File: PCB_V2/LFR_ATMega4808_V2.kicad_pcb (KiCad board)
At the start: 2 copper layers, 51.7 x 63.4 mm, 78 parts, among them J1 Conn_02x02_Odd_Even, J2 Conn_02x05_Odd_Even, J3 Conn_02x02_Counter_Clockwise, J4 Conn_02x02_Counter_Clockwise, J5 Conn_02x02_Counter_Clockwise, J6 Conn_02x03_Odd_Even, J7 Conn_02x02_Odd_Even, Q1 PMOS, Q2 NMOS, Q3 NMOS, Q4 NMOS, Q5 NMOS, Q6 NMOS, Q6 PMOS, Q7 NMOS, Q8 NMOS, U1 ATmega4808-A, U5 MCP1700x-330xxTO

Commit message: Rough layout done
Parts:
- removed the Q6 at (116.6, 106.2)
- removed the Q6 at (107.7, 93.2)
- removed the Q7 at (107.7, 97.7)
- removed the Q7 at (116.5, 110.6)
- removed the R27 at (102.9, 92.5)
- removed the R27 at (121.5, 115.7)
- removed R28, R29: 10k, Resistor_SMD:R_0805_2012Metric_Pad1.20x1.40mm_HandSolder
- removed R30: 47, Resistor_SMD:R_0805_2012Metric_Pad1.20x1.40mm_HandSolder
- removed S2, S4: MJTP1230, MJTP1230:SW_MJTP1230
- added Q6: PMOS, Package_TO_SOT_SMD:SOT-23-3, F.Cu at (130.5, 92.8)
- added Q7: NMOS, Package_TO_SOT_SMD:SOT-23, F.Cu at (134.9, 115.1)
- added R27: 10k, Resistor_SMD:R_0805_2012Metric_Pad1.20x1.40mm_HandSolder, F.Cu at (130.5, 89.8)
- moved H3 138.8 mm to (65.5, 72.0)
- moved H2 118.6 mm to (65.5, 66.1)
- moved H4 99.4 mm to (65.5, 78.0)
- moved H1 76.8 mm to (65.5, 60.1)
- moved D10 68.3 mm to (186.8, 152.5), turned to 90 degrees
- moved D9 62.3 mm to (179.3, 152.5), turned to 90 degrees
- moved D8 59.1 mm to (172.5, 152.5), turned to 90 degrees
- moved R19 57.7 mm to (186.8, 146.0), turned to 90 degrees
- moved C1 52.2 mm to (122.5, 116.0), turned to 180 degrees
- moved C13 52.0 mm to (130.5, 95.8)
- moved C3 51.0 mm to (156.7, 73.8), turned to 0 degrees
- moved R18 50.4 mm to (179.2, 145.8)
- moved Q5 49.0 mm to (137.5, 97.8), turned to 90 degrees
- moved R26 48.8 mm to (141.5, 96.8)
- moved J3 48.7 mm to (149.0, 150.2), turned to -90 degrees
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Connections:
- C12 pad 1: unconnected-(C12-Pad1) -> GND
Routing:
- net +3.3V: track 109.9 -> 0.00 mm, vias 5 -> 0
- net +4.8V: track 95.6 -> 0.00 mm
- net RESET: track 36.0 -> 0.00 mm
- net Button 1: track 31.3 -> 0.00 mm
- net DTR: track 30.4 -> 0.00 mm, vias 2 -> 0
- net ADC Sensor 3: track 25.8 -> 0.00 mm
- net Net-(D1-A): track 25.5 -> 0.00 mm
- net Net-(D2-A): track 24.6 -> 0.00 mm
- net USART RX: track 24.2 -> 0.00 mm
- net USART TX: track 23.5 -> 0.00 mm
- net GND: track 21.6 -> 0.00 mm, vias 15 -> 0
- net Motor 2: track 20.5 -> 0.00 mm, vias 2 -> 0
- net UPDI Data: track 19.9 -> 0.00 mm
- net Motor 1: track 18.4 -> 0.00 mm, vias 2 -> 0
- net ADC Sensor 2: track 16.7 -> 0.00 mm
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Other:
- board outline removed
- board text removed: "LAB_A/01 B: Peter, Arinze, Antoine, Ollie"
- board text removed: "V1"

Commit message: Everything except for buttons is done
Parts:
- added S2: MJTP1230, MJTP1230_:Switch_Tactile_THT_6x6mm_MJTP1230, F.Cu at (165.5, 104.1)
- added S4: MJTP1230, MJTP1230_:Switch_Tactile_THT_6x6mm_MJTP1230, F.Cu at (165.5, 112.2)
- moved H4 137.0 mm to (178.0, 156.2)
- moved H2 108.0 mm to (172.8, 78.7)
- moved H3 100.7 mm to (120.2, 156.5)
- moved H1 56.1 mm to (119.8, 74.2)
- moved D8 26.8 mm to (174.8, 125.8), turned to 180 degrees
- moved R23 22.2 mm to (169.0, 95.8)
- moved R7 20.6 mm to (168.2, 126.0), turned to 180 degrees
- moved D9 20.4 mm to (174.8, 132.6), turned to 180 degrees
- moved R19 19.7 mm to (168.2, 139.2), turned to 180 degrees
- moved R21 18.9 mm to (172.0, 98.8)
- moved D10 17.9 mm to (174.8, 139.2), turned to 180 degrees
- moved R18 17.3 mm to (168.0, 132.6), turned to 180 degrees
- moved C2 10.1 mm to (121.2, 128.0), turned to 0 degrees
- moved C3 9.71 mm to (150.2, 81.0)
- moved J2 8.98 mm to (146.5, 86.8)
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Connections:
- U1 pad 1: Motor 1 -> Motor 4
- U1 pad 2: Motor 2 -> Motor 3
- U1 pad 32: Brake 1 -> Brake 2
- U1 pad 4: Motor 3 -> Motor 1
- U1 pad 5: Motor 4 -> Motor 2
- U1 pad 9: Brake 2 -> Brake 1
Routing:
- net +4.8V: track 0.00 -> 152.1 mm
- net +3.3V: track 0.00 -> 146.2 mm, vias 0 -> 4
- net RESET: track 0.00 -> 48.3 mm
- net LED Green 2: track 0.00 -> 35.6 mm, vias 0 -> 2
- net ADC Sensor 1: track 0.00 -> 34.4 mm, vias 0 -> 2
- net ADC Sensor 2: track 0.00 -> 30.3 mm, vias 0 -> 2
- net LED Green 1: track 0.00 -> 29.9 mm, vias 0 -> 2
- net ADC Sensor 3: track 0.00 -> 29.1 mm, vias 0 -> 2
- net LED Red: track 0.00 -> 25.2 mm, vias 0 -> 2
- net Brake 2: track 0.00 -> 24.2 mm
- net UPDI Data: track 0.00 -> 22.7 mm
- net USART RX: track 0.00 -> 21.2 mm
- net Motor 2: track 0.00 -> 21.1 mm
- net USART TX: track 0.00 -> 20.5 mm
- net Net-(D3-A): track 0.00 -> 20.3 mm, vias 0 -> 2
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
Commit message: close to being done
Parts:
- moved H1 4.79 mm to (122.6, 78.1)
- moved H4 4.31 mm to (173.7, 155.9)
- moved H3 1.55 mm to (121.8, 156.4)
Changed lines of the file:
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@@
 		)
 		(property "Value" "47"
-			(at 0 1.65 0)
+			(at -0.25 1.65 0)
 			(layer "F.Fab")
 			(effects
@@
 	(footprint "MountingHole:MountingHole_2.2mm_M2"
 		(layer "F.Cu")
-		(at 120.25 156.5)
+		(at 121.8 156.4)
 		(descr "Mounting Hole 2.2mm, M2, no annular, generated by kicad-footprint-generator mountinghole.py")
 		(tags "mountinghole M2")
@@
 		)
 		(property "Value" "NMOS"
-			(at 0 2.4 90)
+			(at 0 2.3 90)
 			(layer "F.Fab")
 			(effects
@@
 	(footprint "MountingHole:MountingHole_2.2mm_M2"
 		(layer "F.Cu")
-		(at 119.75 74.25)
+		(at 122.6 78.1)
 		(descr "Mounting Hole 2.2mm, M2, no annular, generated by kicad-footprint-generator mountinghole.py")
 		(tags "mountinghole M2")
@@
 	(footprint "MountingHole:MountingHole_2.2mm_M2"
 		(layer "F.Cu")
-		(at 178 156.25)
+		(at 173.7 155.9)
 		(descr "Mounting Hole 2.2mm, M2, no annular, generated by kicad-footprint-generator mountinghole.py")
 		(tags "mountinghole M2")

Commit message: Finished the wiring, now on to the silkscreen
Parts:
- BT1: footprint Connector_PinSocket_1.00mm:PinSocket_1x02_P1.00mm_Vertical_SMD_Pin1Left -> Connector_PinHeader_2.54mm:PinHeader_1x02_P2.54mm_Vertical
- H1, H2, H3, H4: footprint MountingHole:MountingHole_2.2mm_M2 -> MountingHole:MountingHole_2.2mm_M2_Pad
- moved R21 17.3 mm to (172.5, 116.0), turned to 90 degrees
- moved R23 16.6 mm to (172.5, 112.0), turned to -90 degrees
- moved S2 13.2 mm to (170.0, 116.5), turned to 180 degrees
- moved S4 7.62 mm to (170.0, 106.0), turned to 180 degrees
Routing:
- net Button 1: track 0.00 -> 26.1 mm, vias 0 -> 1
- net RESET: track 48.3 -> 63.8 mm
- net GND: track 8.55 -> 17.6 mm, vias 7 -> 17

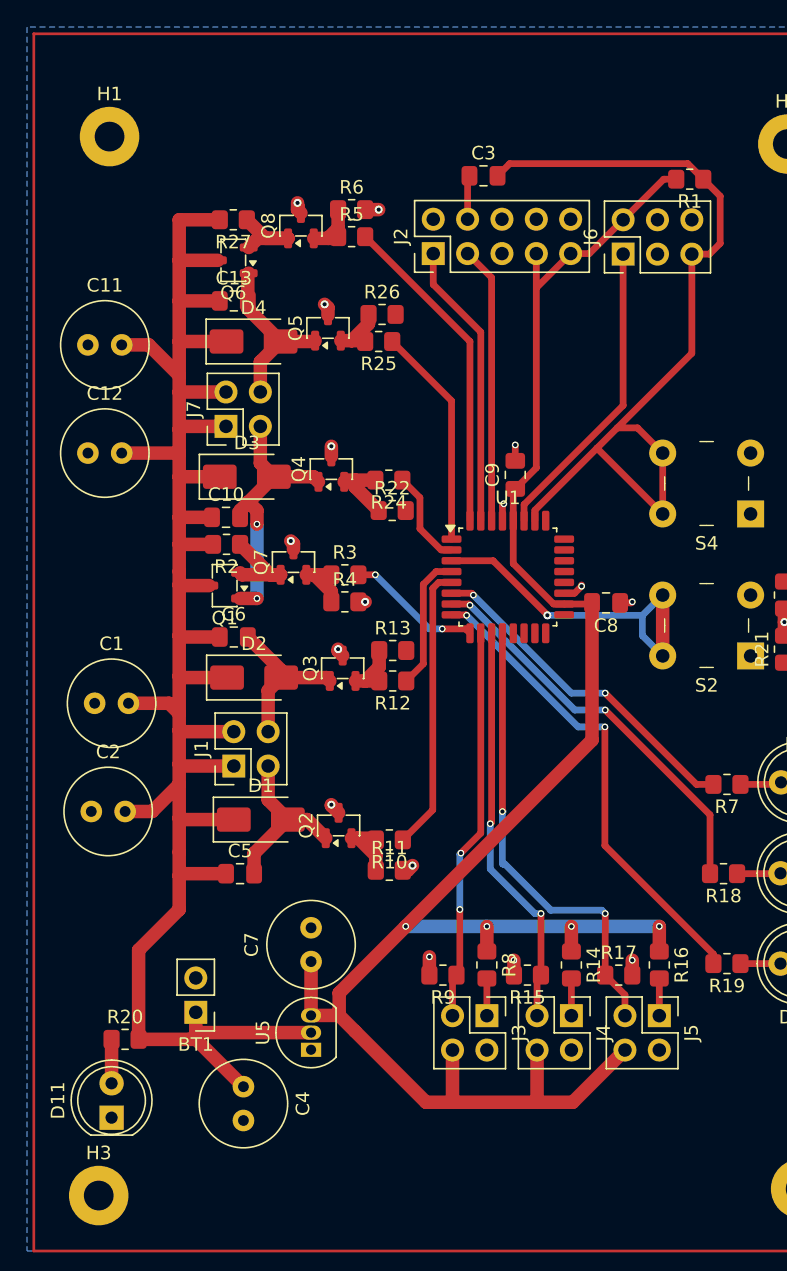
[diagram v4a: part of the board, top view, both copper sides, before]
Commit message: Changed sensors to take input from a separate PCB
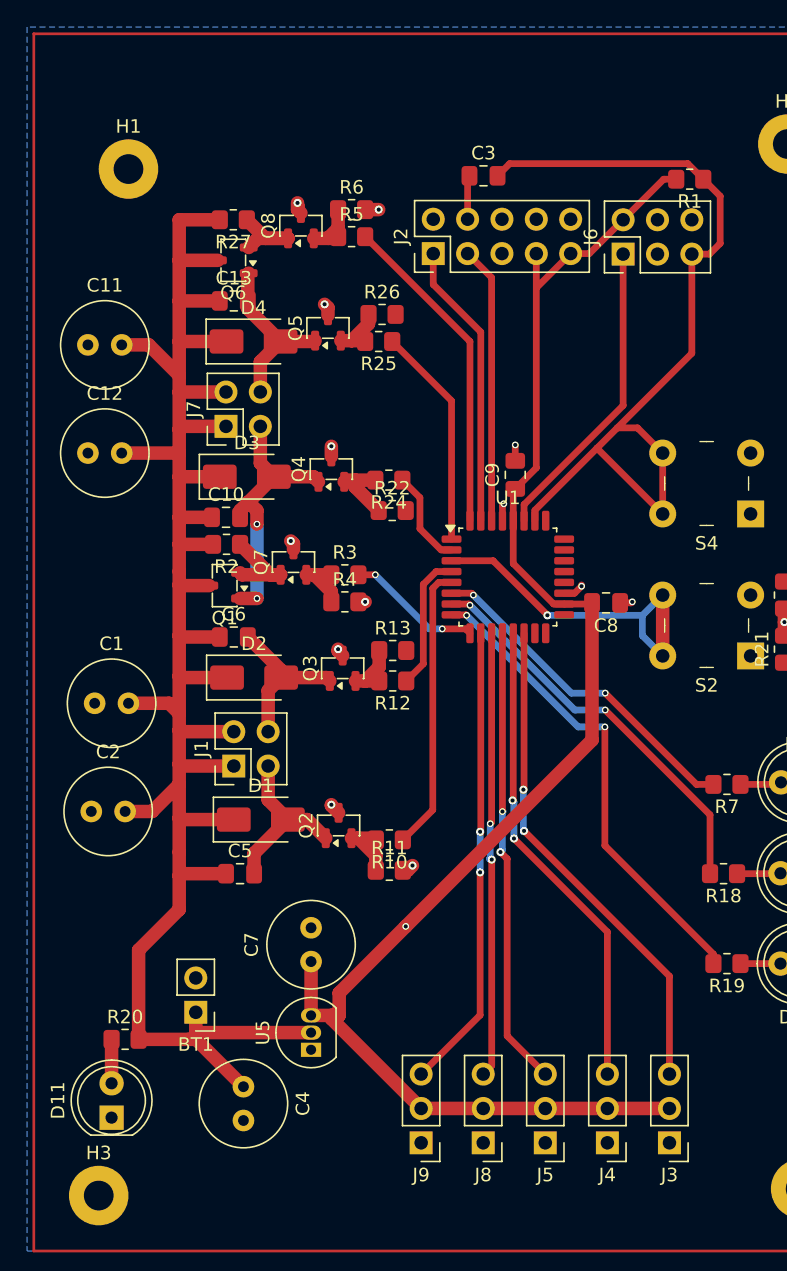
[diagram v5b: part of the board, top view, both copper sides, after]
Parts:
- removed R14, R16, R8: 68, Resistor_SMD:R_0805_2012Metric_Pad1.20x1.40mm_HandSolder
- removed R15, R17, R9: 10k, Resistor_SMD:R_0805_2012Metric_Pad1.20x1.40mm_HandSolder
- added J8: Conn_01x03, Connector_PinHeader_2.54mm:PinHeader_1x03_P2.54mm_Vertical, F.Cu at (150.2, 152.5)
- added J9: Conn_01x03, Connector_PinHeader_2.54mm:PinHeader_1x03_P2.54mm_Vertical, F.Cu at (145.6, 152.5)
- J3, J4, J5: value Conn_02x02_Counter_Clockwise -> Conn_01x03; footprint Connector_PinHeader_2.54mm:PinHeader_2x02_P2.54mm_Vertical -> Connector_PinHeader_2.54mm:PinHeader_1x03_P2.54mm_Vertical
- moved J3 16.5 mm to (164.0, 152.5), turned to 180 degrees
- moved J5 12.6 mm to (154.8, 152.5), turned to 180 degrees
- moved J4 9.77 mm to (159.4, 152.5), turned to 180 degrees
- moved H1 2.78 mm to (124.0, 80.5)
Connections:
- J3 pad 1: Net-(J3-Pin_1) -> GND
- J3 pad 2: GND -> +3.3V
- J3 pad 3: ADC Sensor 3 -> ADC Sensor 5
- J4 pad 1: Net-(J4-Pin_1) -> GND
- J4 pad 2: GND -> +3.3V
- J4 pad 3: ADC Sensor 2 -> ADC Sensor 4
- J5 pad 1: Net-(J5-Pin_1) -> GND
- J5 pad 2: GND -> +3.3V
- J5 pad 3: ADC Sensor 1 -> ADC Sensor 3
- U1 pad 10: ADC Sensor 3 -> ADC Sensor 1
- U1 pad 12: ADC Sensor 1 -> ADC Sensor 3
- U1 pad 13: unconnected-(U1-PD3-Pad13) -> ADC Sensor 4
- U1 pad 14: unconnected-(U1-PD4-Pad14) -> ADC Sensor 5
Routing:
- net ADC Sensor 5: track 0.00 -> 37.4 mm, vias 0 -> 2
- net ADC Sensor 4: track 0.00 -> 35.6 mm, vias 0 -> 2
- net +3.3V: track 146.2 -> 116.7 mm, vias 4 -> 1
- net ADC Sensor 3: track 29.1 -> 34.1 mm
- net GND: track 17.6 -> 14.0 mm, vias 17 -> 14
- net ADC Sensor 2: track 30.3 -> 33.0 mm
- net Net-(J5-Pin_1): track 2.75 -> 0.00 mm
- net Net-(J4-Pin_1): track 2.75 -> 0.00 mm
- net Net-(J3-Pin_1): track 2.75 -> 0.00 mm

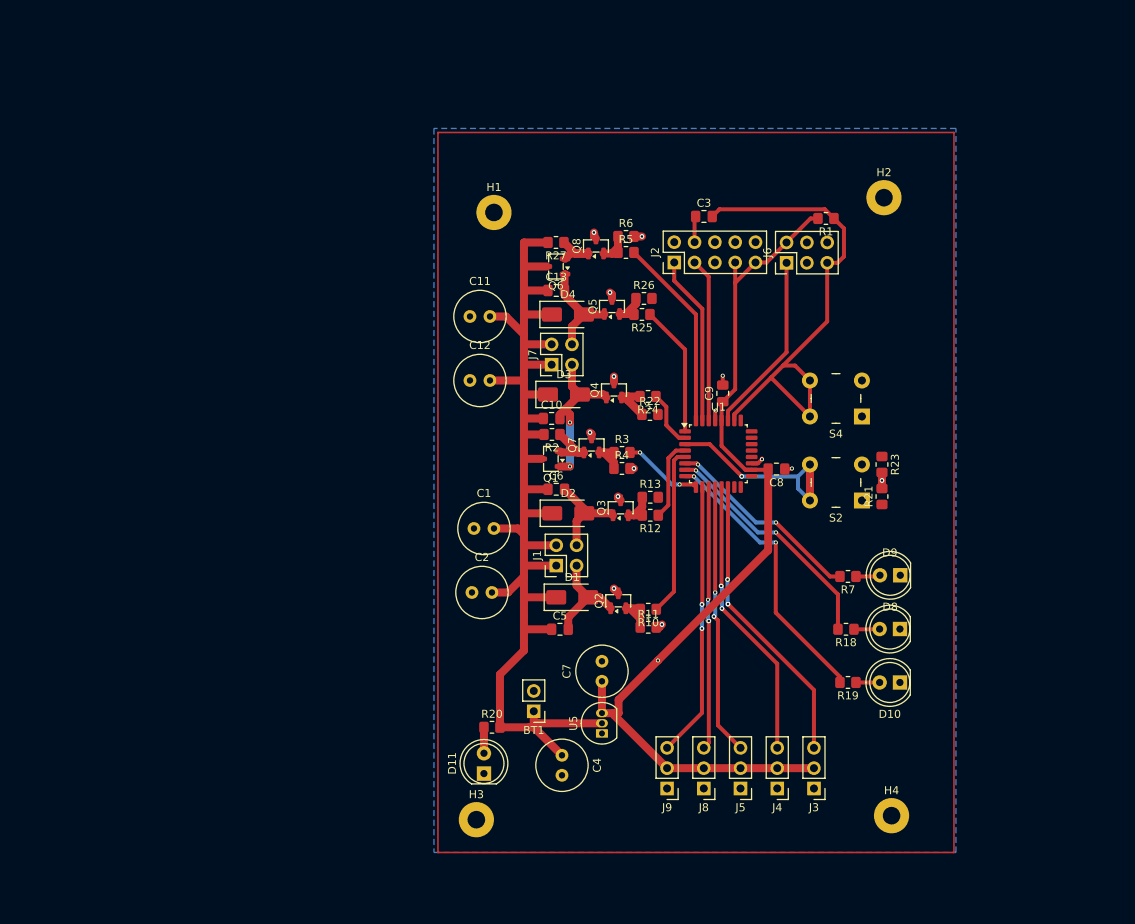
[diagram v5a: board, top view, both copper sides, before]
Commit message: Finished silk screen, no erros, 2 warnings with footprints
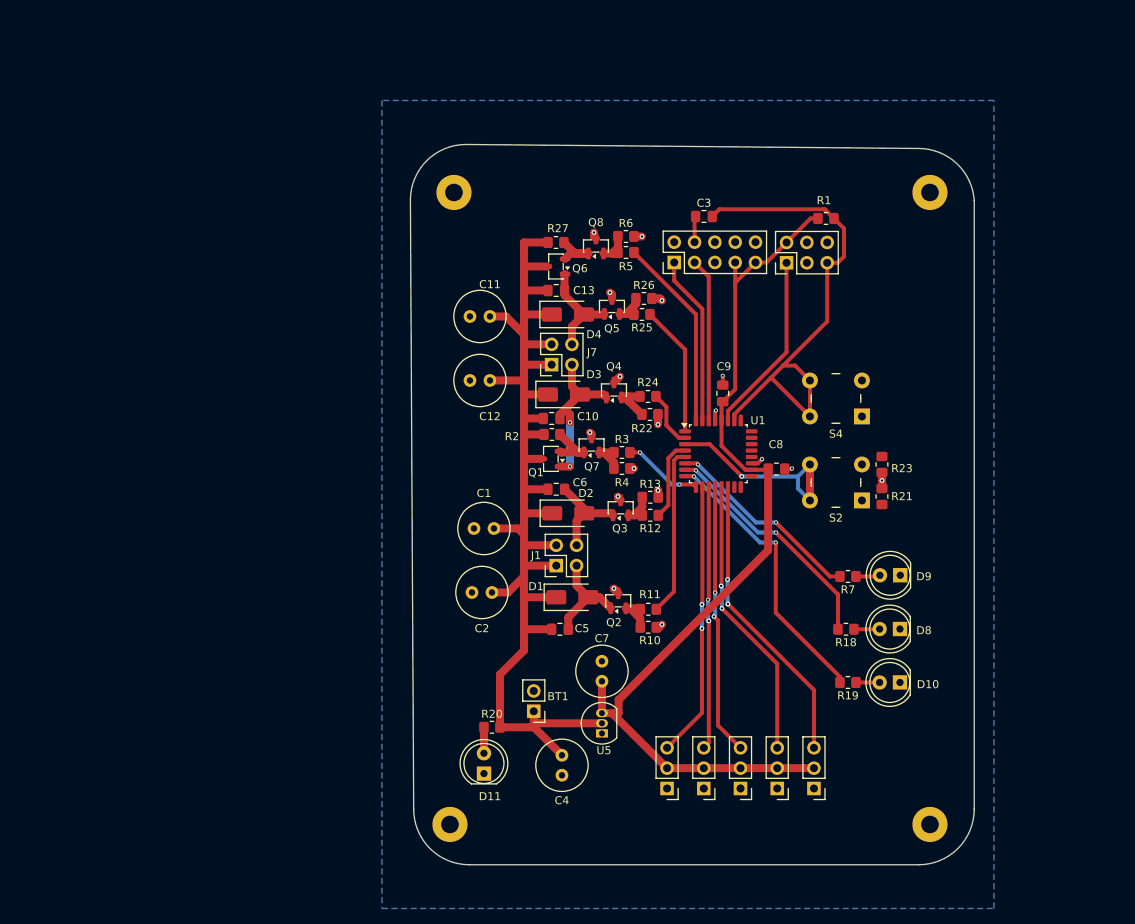
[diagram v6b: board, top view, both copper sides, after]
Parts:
- moved H2 5.79 mm to (178.5, 78.0)
- moved H1 5.59 mm to (119.0, 78.0)
- moved H4 4.92 mm to (178.5, 157.0)
- moved H3 3.35 mm to (118.5, 157.0)
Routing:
- net GND: track 14.0 -> 17.8 mm, vias 14 -> 17
- net +3.3V: vias 1 -> 0
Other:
- board outline added: 70.5 x 90 mm

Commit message: Everything done, checking footprints are correct
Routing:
- net Net-(R23-Pad1): track 0.00 -> 2.91 mm
- net Net-(R21-Pad1): track 0.00 -> 2.71 mm
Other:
- board text added: "LabA/01 B: Peter, Arinze, Antoine, Ollie"
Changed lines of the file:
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@@
 		(layer "Edge.Cuts")
+	)
+	(gr_text "LabA/01 B: Peter, Arinze, Antoine, Ollie"
+		(at 170.5 77 0)
+		(layer "B.SilkS")
+		(effects
+			(font
+				(size 1.5 1.5)
+				(thickness 0.3)
+				(bold yes)
+			)
+			(justify left bottom mirror)
+		)
 	)
 	(segment
@@
 	)
 	(segment
+		(start 172.5 111)
+		(end 171 111)
+		(width 1)
+		(layer "F.Cu")
+		(net "Net-(R23-Pad1)")
+	)
+	(segment
+		(start 171 111)
+		(end 170 112)
+		(width 1)
+		(layer "F.Cu")
+		(net "Net-(R23-Pad1)")
+	)
+	(segment
 		(start 153.199999 126.456499)
 		(end 153.199999 126.385787)
@@
 	)
 	(segment
+		(start 172.5 117)
+		(end 170.5 117)
+		(width 1)
+		(layer "F.Cu")
+		(net "Net-(R21-Pad1)")
+	)
+	(segment
+		(start 170.5 117)
+		(end 170 116.5)
+		(width 1)
+		(layer "F.Cu")
+		(net "Net-(R21-Pad1)")
+	)
+	(segment
